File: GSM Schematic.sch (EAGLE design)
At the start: 12 parts, among them IC1 7805T, J1 5.5x2.1mm Barrel, Q1 16M, U1 ATMEGA328P-PU

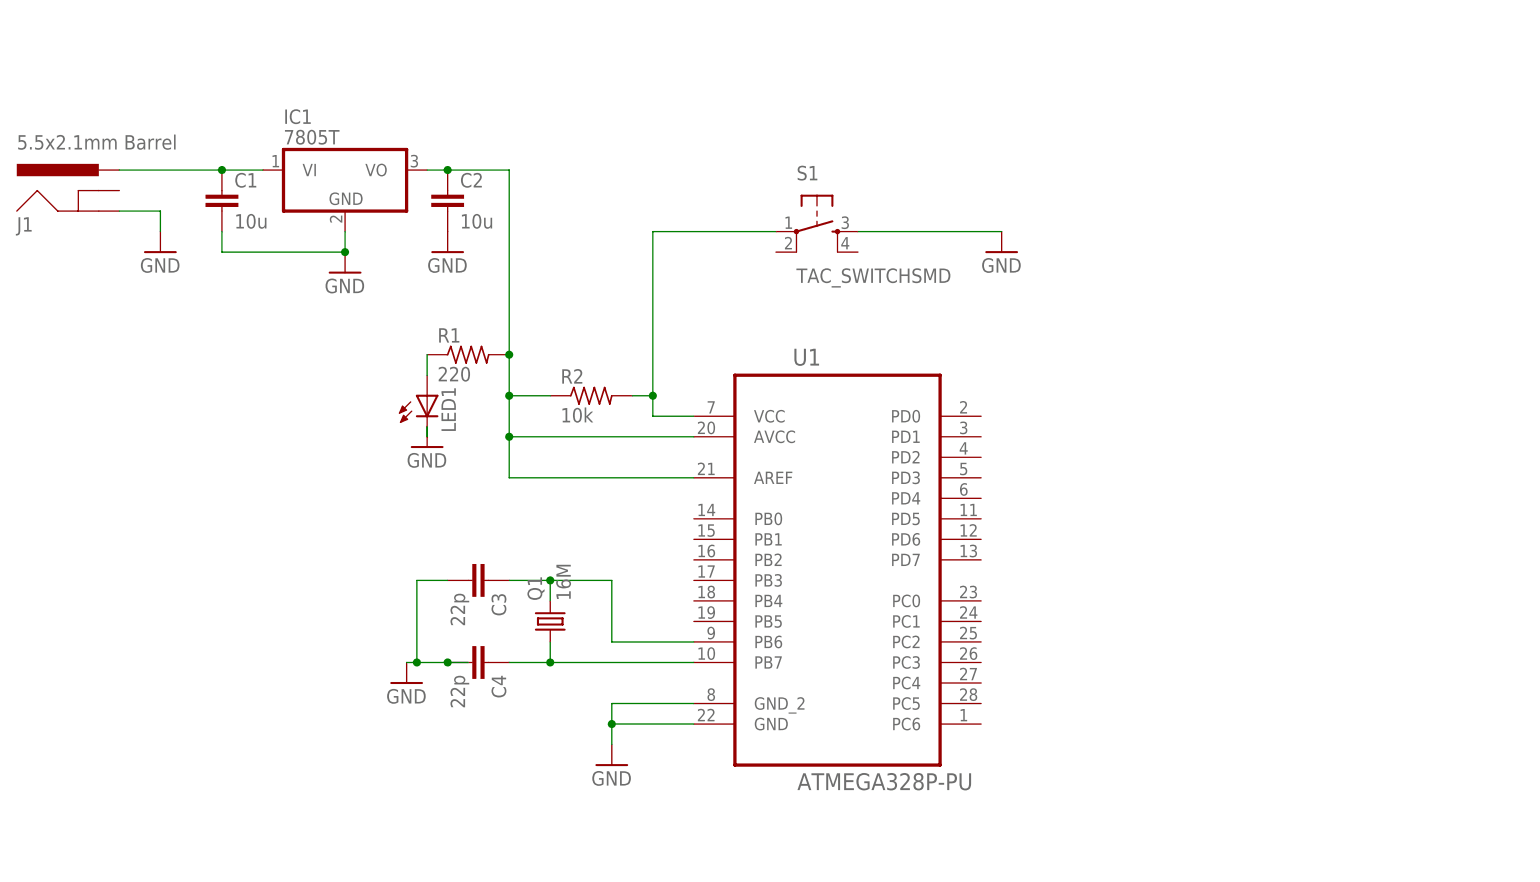
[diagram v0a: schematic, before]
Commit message: Cleaned up the schematic and fixed ERC errors
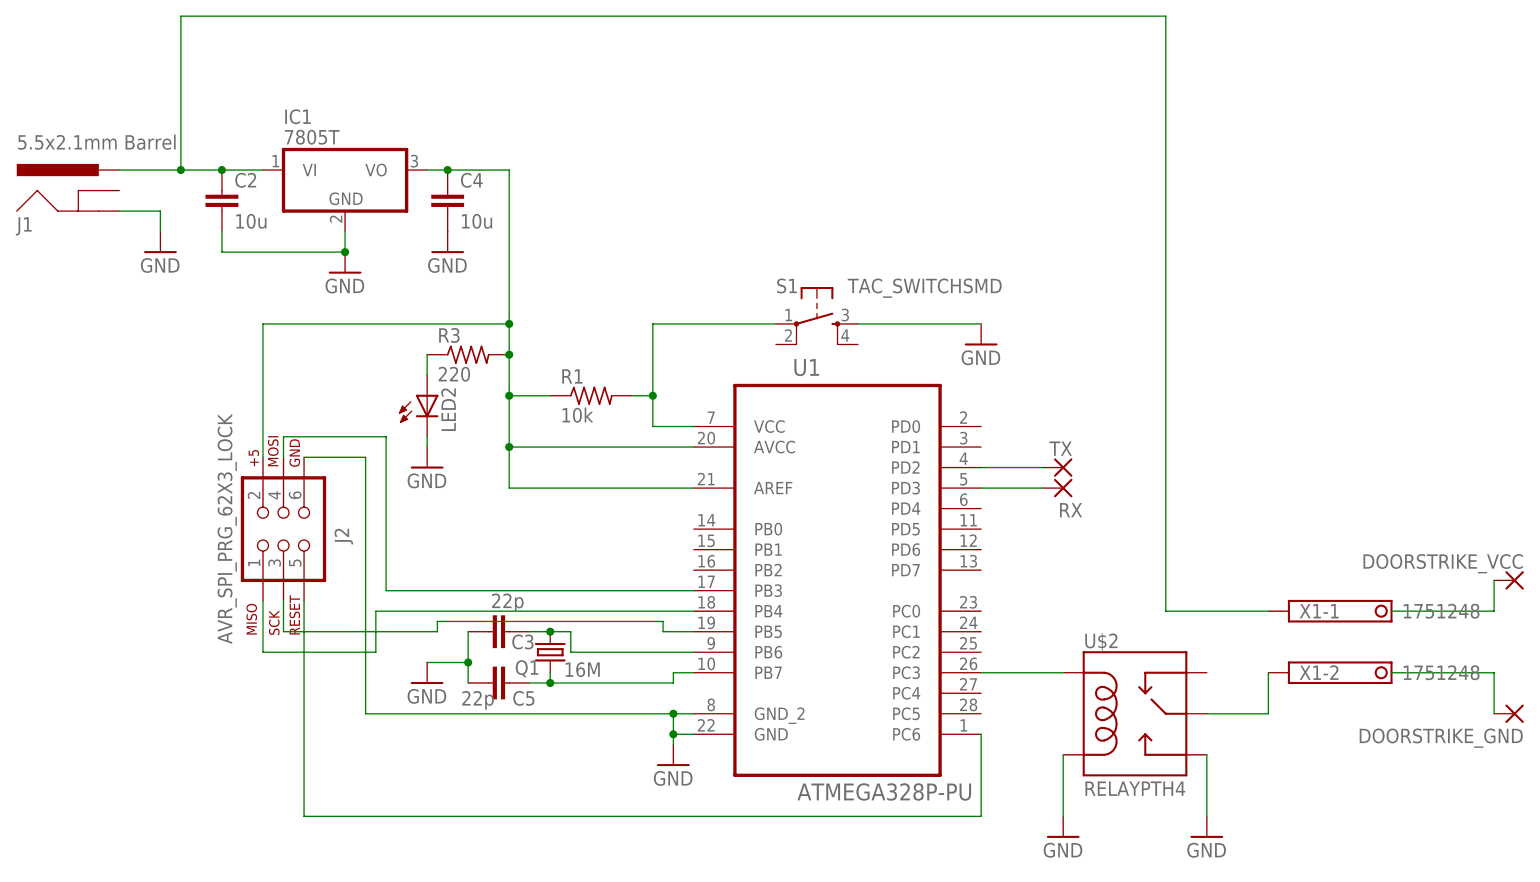
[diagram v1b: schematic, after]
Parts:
- removed C1: 10u, rcl:C-EU025-024X044
- removed LED1: (no value), led:LED5MM
- removed R2: 10k, rcl:R-US_0204/5
- added C5: 22p, rcl:C-EUC0603
- added DOORSTRIKE_GND, DOORSTRIKE_VCC, RX, TX: (no value), wirepad:2,54/0,9
- added J2: AVR_SPI_PRG_62X3_LOCK, SparkFun-Connectors:AVR_SPI_PRG_62X3_LOCK
- added LED2: (no value), led:LEDSML0603
- added R3: 220, rcl:R-US_R0603
- added U$2: RELAYPTH4, SparkFun-Electromechanical:RELAYPTH4
- added X1: 1751248, con-phoenix-350:1751248
- C2, C3: device rcl:C-EU025-024X044 -> rcl:C-EUC0603
- C4: value 22p -> 10u; device rcl:C-EU025-024X044 -> rcl:C-EUC0603
- R1: value 220 -> 10k; device rcl:R-US_0204/5 -> rcl:R-US_R0603
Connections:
- new net N$10: J2.5, U1.PC6
- new net N$11: C4.1, IC1.VO, J2.2, R1.1, R3.2, U1.AREF, U1.AVCC
- new net N$12: RX.P, U1.PD3
- new net N$13: U$2.MAIN, X1-2.K
- new net N$14: U$2.COIL1, U1.PC3
- new net N$15: DOORSTRIKE_VCC.P
- new net N$16: DOORSTRIKE_GND.P
- new net N$7: J2.4, U1.PB3
- new net N$8: J2.1, U1.PB4
- new net N$9: J2.3, U1.PB5
- net GND: now also C5.2, J2.6, LED2.C, U$2.COIL2, U$2.NO; no longer C1.2, LED1.C
- net N$1: now also TX.P, U1.PD2; no longer C2.1, IC1.VO, R1.2, R2.1, U1.AREF, U1.AVCC
- net N$2: now also R1.2; no longer R2.2
- net N$3: now also LED2.A, R3.1; no longer LED1.A, R1.1
- net N$4: now also C5.1; no longer C4.1
- net N$6: now also C2.1, X1-1.K; no longer C1.1
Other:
- moved on the sheet: C2, C3, C4, Q1, R1, S1, U1

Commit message: Update GSM Schematic.sch
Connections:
- net N$6: now also U$2.NC
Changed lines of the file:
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@@
 <setting verticaltext="up"/>
 </settings>
-<grid distance="0.1" unitdist="inch" unit="inch" style="lines" multiple="1" display="yes" altdistance="0.01" altunitdist="inch" altunit="inch"/>
+<grid distance="0.1" unitdist="inch" unit="inch" style="lines" multiple="1" display="no" altdistance="0.01" altunitdist="inch" altunit="inch"/>
 <layers>
 <layer number="1" name="Top" color="4" fill="1" visible="no" active="no"/>
@@
 <wire x1="276.86" y1="223.52" x2="154.94" y2="223.52" width="0.1524" layer="91"/>
 <pinref part="X1" gate="-1" pin="K"/>
-<wire x1="289.56" y1="149.86" x2="276.86" y2="149.86" width="0.1524" layer="91"/>
+<wire x1="289.56" y1="149.86" x2="281.94" y2="149.86" width="0.1524" layer="91"/>
+<wire x1="281.94" y1="149.86" x2="276.86" y2="149.86" width="0.1524" layer="91"/>
 <wire x1="276.86" y1="223.52" x2="276.86" y2="149.86" width="0.1524" layer="91"/>
-</segment>
-</net>
+<pinref part="U$2" gate="K$1" pin="NC"/>
+<wire x1="281.94" y1="142.24" x2="281.94" y2="149.86" width="0.1524" layer="91"/>
+<junction x="281.94" y="149.86"/>
+</segment>
+</net>

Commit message: Add files via upload
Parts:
- removed C3, C5: 22p, rcl:C-EUC0603
- removed Q1: 16M, crystal:CRYSTALHC49UP
- removed U$2: RELAYPTH4, SparkFun-Electromechanical:RELAYPTH4
- added C1, C6: 22p, rcl:C-EUC0603
- added Q2: 16M, crystal:CRYSTALHC49UP
- added SPDT: RELAYPTH4, SparkFun-Electromechanical:RELAYPTH4
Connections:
- removed net N$4: C5.1, Q1.1, U1.PB7
- removed net N$5 (its old number): C3.1, Q1.2, U1.PB6
- removed net N$6 (its old number): C2.1, IC1.VI, J1.PWR, U$2.NC, X1-1.K
- new net N$16: C1.1, Q2.2, U1.PB6
- new net N$17: C2.1, IC1.VI, J1.PWR, SPDT.NC, X1-1.K
- new net N$18: C6.1, Q2.1, U1.PB7
- net GND: now also C1.2, C6.2, SPDT.COIL2, SPDT.NO; no longer C3.2, C5.2, U$2.COIL2, U$2.NO
- net N$13: now also SPDT.MAIN; no longer U$2.MAIN
- net N$14: now also SPDT.COIL1; no longer U$2.COIL1
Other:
- note added: "1"
- note added: "4"
- moved on the sheet: C2, C4, DOORSTRIKE_GND, DOORSTRIKE_VCC, IC1, J1, J2, LED2, R1, R3, S1

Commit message: Add files via upload
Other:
- note added: "5"
- note removed: "4"
- moved on the sheet: LED2, R1, R3
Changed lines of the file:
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@@
 <sheet>
 <plain>
-<text x="419.1" y="7.62" size="1.778" layer="91">4</text>
 <text x="330.2" y="7.62" size="1.778" layer="91">1</text>
+<text x="419.1" y="7.62" size="1.778" layer="91">5</text>
 </plain>
 <instances>
@@
 <instance part="IC1" gate="A1" x="175.26" y="205.74"/>
 <instance part="GND1" gate="1" x="175.26" y="193.04"/>
-<instance part="GND2" gate="1" x="185.42" y="165.1" smashed="yes">
-<attribute name="VALUE" x="182.88" y="162.56" size="1.778" layer="96"/>
+<instance part="GND2" gate="1" x="185.42" y="161.29" smashed="yes">
+<attribute name="VALUE" x="182.88" y="158.75" size="1.778" layer="96"/>
 </instance>
 <instance part="GND3" gate="1" x="187.96" y="193.04"/>
@@
 <instance part="FRAME1" gate="G$1" x="0" y="0"/>
 <instance part="FRAME1" gate="G$2" x="325.12" y="0"/>
-<instance part="R3" gate="G$1" x="190.5" y="179.07" smashed="yes">
-<attribute name="NAME" x="189.23" y="181.8386" size="1.778" layer="95"/>
-<attribute name="VALUE" x="189.23" y="175.768" size="1.778" layer="96"/>
-</instance>
-<instance part="R1" gate="G$1" x="205.74" y="175.26" smashed="yes">
-<attribute name="NAME" x="204.47" y="178.0286" size="1.778" layer="95"/>
-<attribute name="VALUE" x="204.47" y="171.958" size="1.778" layer="96"/>
+<instance part="R3" gate="G$1" x="190.5" y="177.8" smashed="yes">
+<attribute name="NAME" x="189.23" y="180.5686" size="1.778" layer="95"/>
+<attribute name="VALUE" x="189.23" y="174.498" size="1.778" layer="96"/>
+</instance>
+<instance part="R1" gate="G$1" x="205.74" y="177.8" smashed="yes">
+<attribute name="NAME" x="204.47" y="180.5686" size="1.778" layer="95"/>
+<attribute name="VALUE" x="204.47" y="174.498" size="1.778" layer="96"/>
 </instance>
 <instance part="C4" gate="G$1" x="187.96" y="203.2"/>
 <instance part="C2" gate="G$1" x="160.02" y="203.2"/>
-<instance part="LED2" gate="G$1" x="185.42" y="173.99" smashed="yes">
-<attribute name="NAME" x="181.102" y="173.736" size="1.778" layer="95" rot="R180"/>
-<attribute name="VALUE" x="191.135" y="169.418" size="1.778" layer="96" rot="R90"/>
+<instance part="LED2" gate="G$1" x="185.42" y="170.18" smashed="yes">
+<attribute name="NAME" x="181.102" y="169.926" size="1.778" layer="95" rot="R180"/>
+<attribute name="VALUE" x="191.135" y="165.608" size="1.778" layer="96" rot="R90"/>
 </instance>
 <instance part="J2" gate="G$1" x="154.94" y="162.56" smashed="yes">
@@
 <segment>
 <pinref part="GND2" gate="1" pin="GND"/>
-<wire x1="185.42" y1="167.64" x2="185.42" y2="168.91" width="0.1524" layer="91"/>
+<wire x1="185.42" y1="163.83" x2="185.42" y2="165.1" width="0.1524" layer="91"/>
 <pinref part="LED2" gate="G$1" pin="C"/>
 </segment>
@@
 <pinref part="R3" gate="G$1" pin="1"/>
 <pinref part="LED2" gate="G$1" pin="A"/>
-<wire x1="185.42" y1="176.53" x2="185.42" y2="179.07" width="0.1524" layer="91"/>
+<wire x1="185.42" y1="172.72" x2="185.42" y2="177.8" width="0.1524" layer="91"/>
 </segment>
 </net>
@@
 <segment>
 <pinref part="S1" gate="S" pin="1"/>
-<wire x1="215.9" y1="175.26" x2="215.9" y2="185.42" width="0.1524" layer="91"/>
+<wire x1="215.9" y1="177.8" x2="215.9" y2="185.42" width="0.1524" layer="91"/>
 <wire x1="215.9" y1="185.42" x2="231.14" y2="185.42" width="0.1524" layer="91"/>
-<wire x1="215.9" y1="175.26" x2="210.82" y2="175.26" width="0.1524" layer="91"/>
-<junction x="215.9" y="175.26"/>
+<wire x1="215.9" y1="177.8" x2="210.82" y2="177.8" width="0.1524" layer="91"/>
+<junction x="215.9" y="177.8"/>
 <pinref part="U1" gate="A" pin="VCC"/>
-<wire x1="215.9" y1="175.26" x2="215.9" y2="172.72" width="0.1524" layer="91"/>
+<wire x1="215.9" y1="177.8" x2="215.9" y2="172.72" width="0.1524" layer="91"/>
 <wire x1="215.9" y1="172.72" x2="218.44" y2="172.72" width="0.1524" layer="91"/>
 <pinref part="R1" gate="G$1" pin="2"/>
@@
 <wire x1="187.96" y1="205.74" x2="195.58" y2="205.74" width="0.1524" layer="91"/>
 <wire x1="195.58" y1="205.74" x2="195.58" y2="185.42" width="0.1524" layer="91"/>
-<wire x1="195.58" y1="185.42" x2="195.58" y2="179.07" width="0.1524" layer="91"/>
-<wire x1="195.58" y1="179.07" x2="195.58" y2="175.26" width="0.1524" layer="91"/>
-<wire x1="195.58" y1="170.18" x2="195.58" y2="175.26" width="0.1524" layer="91"/>
-<wire x1="200.66" y1="175.26" x2="195.58" y2="175.26" width="0.1524" layer="91"/>
-<junction x="195.58" y="175.26"/>
+<wire x1="195.58" y1="185.42" x2="195.58" y2="177.8" width="0.1524" layer="91"/>
+<wire x1="195.58" y1="170.18" x2="195.58" y2="177.8" width="0.1524" layer="91"/>
+<wire x1="200.66" y1="177.8" x2="195.58" y2="177.8" width="0.1524" layer="91"/>
+<junction x="195.58" y="177.8"/>
 <pinref part="U1" gate="A" pin="AVCC"/>
 <wire x1="218.44" y1="170.18" x2="215.9" y2="170.18" width="0.1524" layer="91"/>
 <pinref part="R3" gate="G$1" pin="2"/>
-<junction x="195.58" y="179.07"/>
+<junction x="195.58" y="177.8"/>
 <pinref part="R1" gate="G$1" pin="1"/>
 <pinref part="C4" gate="G$1" pin="1"/>

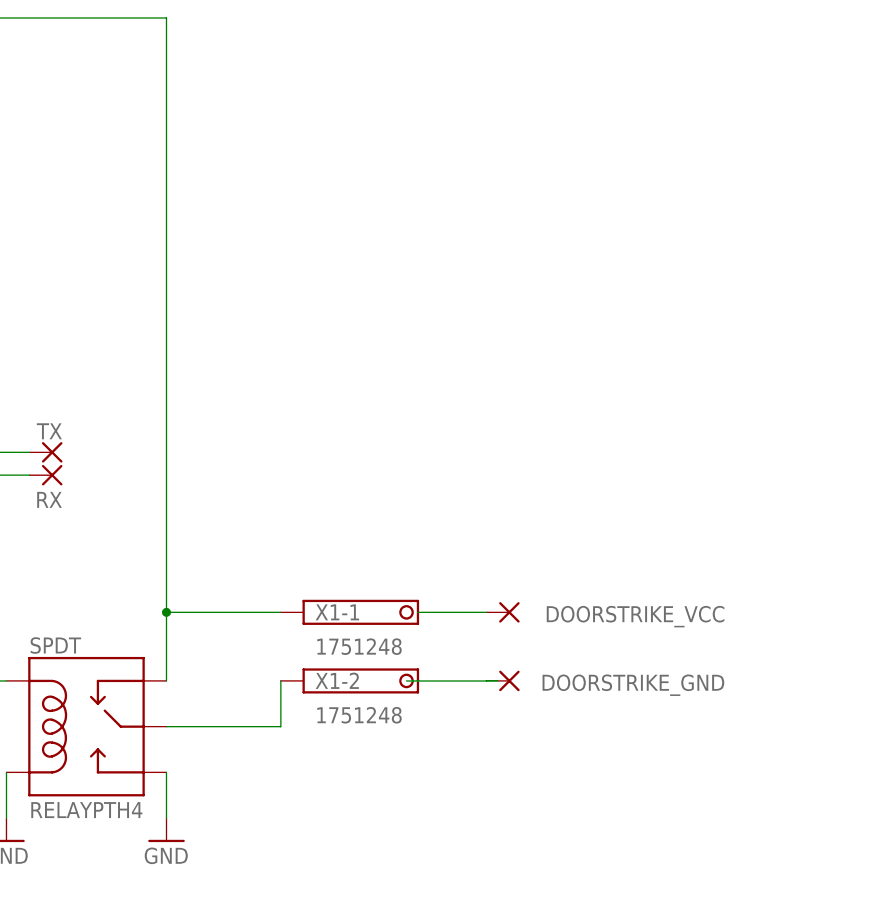
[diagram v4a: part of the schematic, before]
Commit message: Add files via upload
Fixed the relay to door strike connection and replaced terminals with 237-102 WAGO terminal blocks
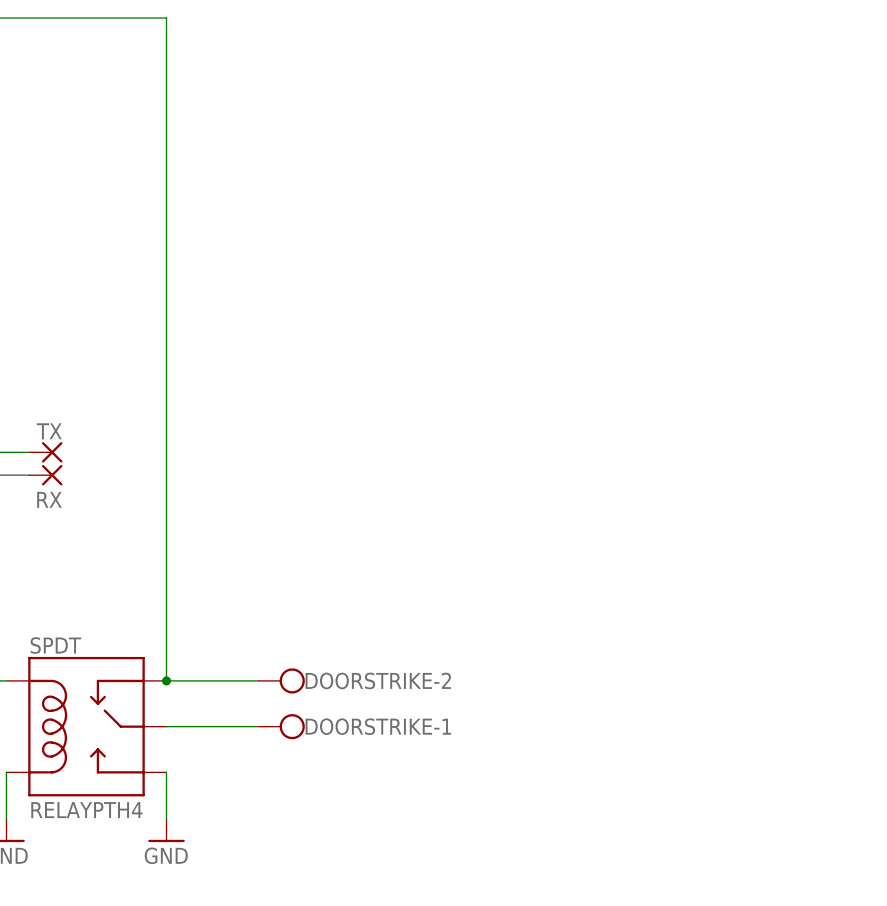
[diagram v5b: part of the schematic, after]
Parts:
- removed DOORSTRIKE_GND, DOORSTRIKE_VCC: (no value), wirepad:2,54/0,9
- removed X1: 1751248, con-phoenix-350:1751248
- added DOORSTRIKE: (no value), con-wago-500:W237-102
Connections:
- removed net N$13: SPDT.MAIN, X1-2.K
- removed net N$15: DOORSTRIKE_VCC.P
- removed net N$6: DOORSTRIKE_GND.P
- new net N$4: DOORSTRIKE-1.KL, SPDT.MAIN
- net N$17: now also DOORSTRIKE-2.KL; no longer X1-1.K

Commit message: Add files via upload
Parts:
- added LED1: (no value), led:LEDSML0603
- added R2: 220, rcl:R-US_R0603
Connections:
- new net N$6: LED1.A, R2.2
- new net N$9: R2.1
- net GND: now also LED1.C
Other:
- note added: "7"
- note removed: "5"
- moved on the sheet: C1, C6
